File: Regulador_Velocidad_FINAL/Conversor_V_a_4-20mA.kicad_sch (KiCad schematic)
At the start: 10 parts, among them J3 Salida 4-20 mA, Q3 PN2222A, U4 TL082, U6 TL082

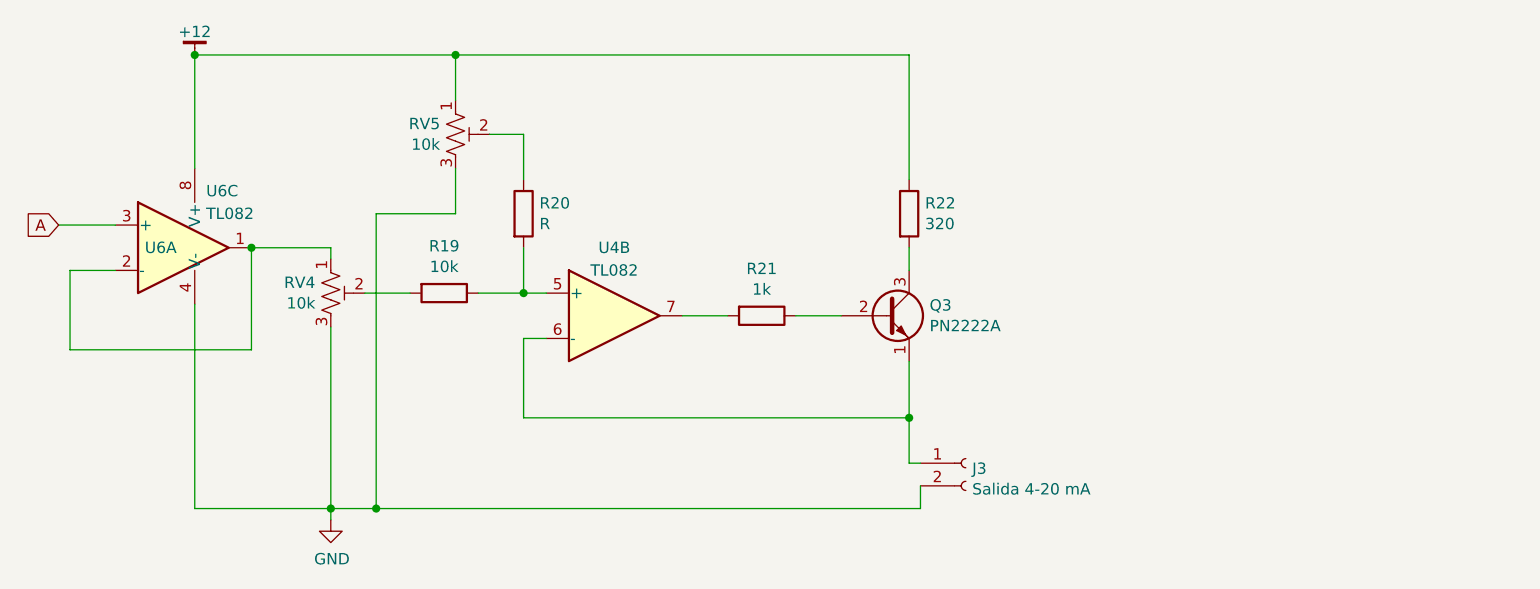
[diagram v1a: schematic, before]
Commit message: Speed_Monitor: Changes on schematics
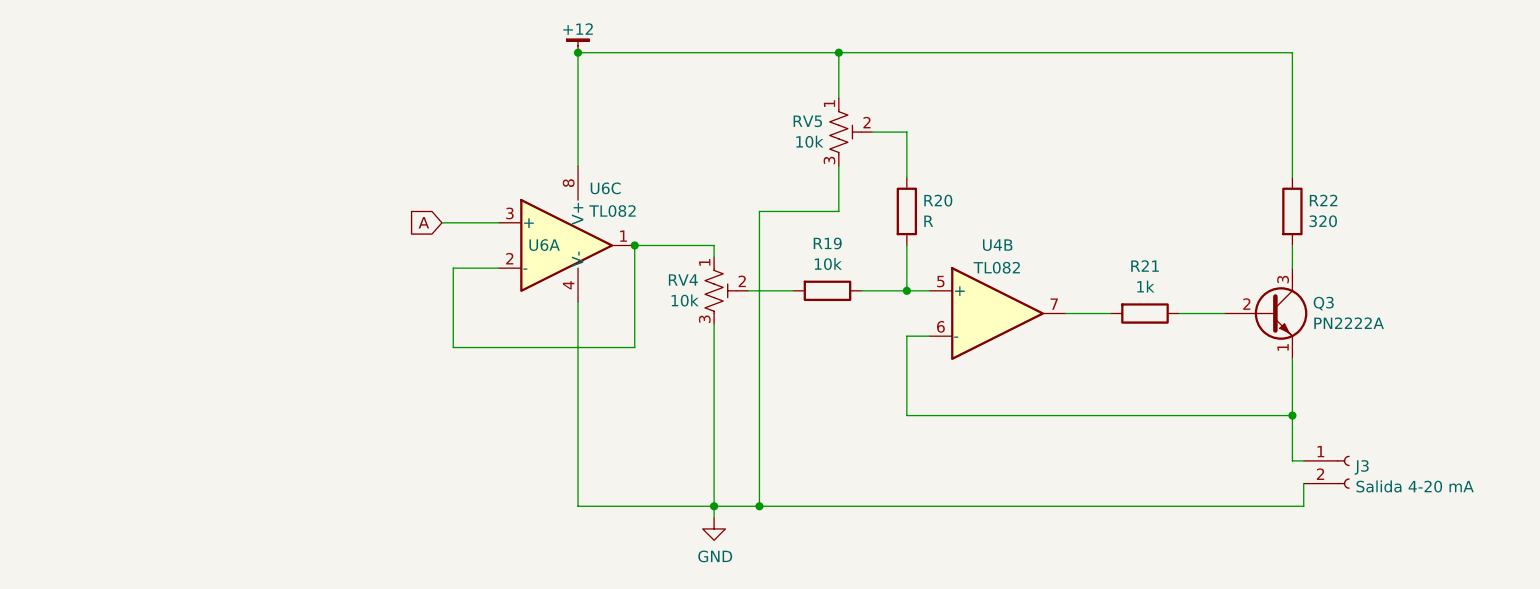
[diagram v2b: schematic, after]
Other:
- moved on the sheet: J3, Q3, R19, R20, R21, R22, RV4, RV5, U4B, U6A, U6C
